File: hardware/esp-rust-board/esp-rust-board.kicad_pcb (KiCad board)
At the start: 2 copper layers, 22.9 x 63.5 mm, 96 parts, among them J1 USB4105-GF-A, Q1 DMG3415U, SW1 SW_Push, SW2 SW_Push, U1 SHTC3, U2 ICM-42670-P, U3 ESP32-C3-MINI-1, U4 Rust_Board, U5 SY8088, U6 MCP73831T-2ACI/OT, Y1 32.768Hz

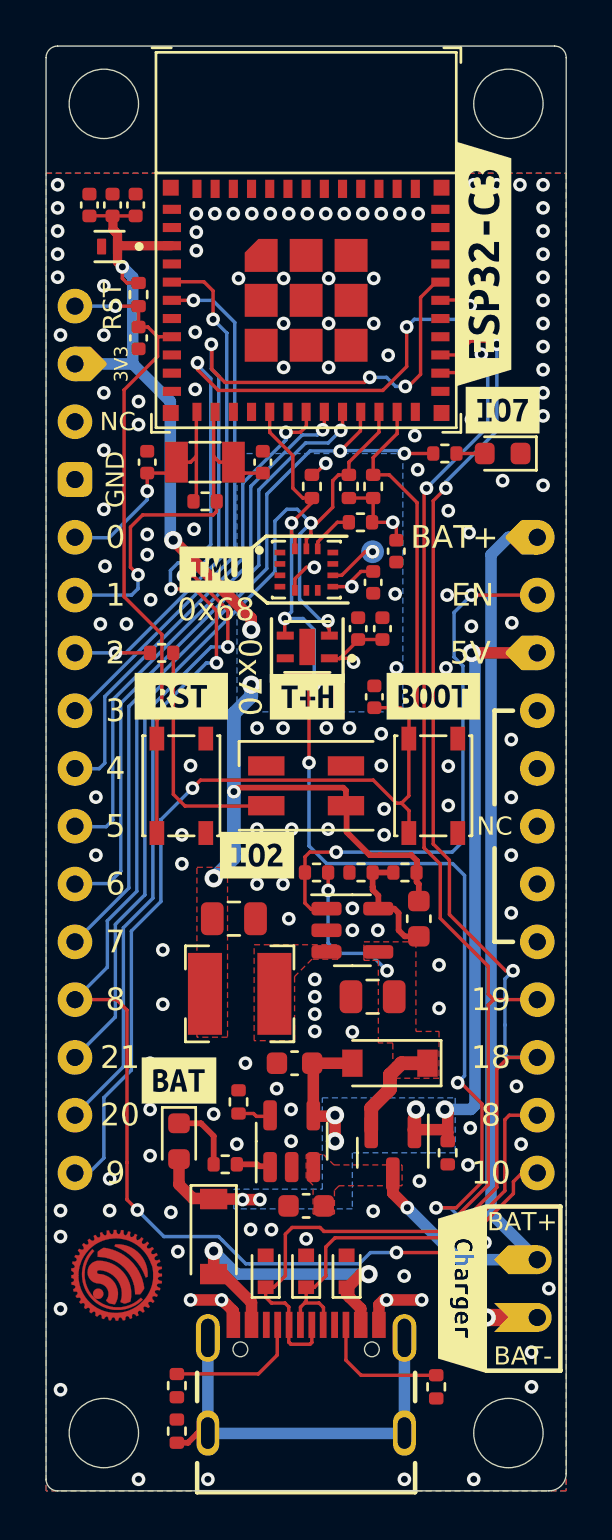
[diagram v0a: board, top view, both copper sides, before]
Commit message: Added LIS3DH
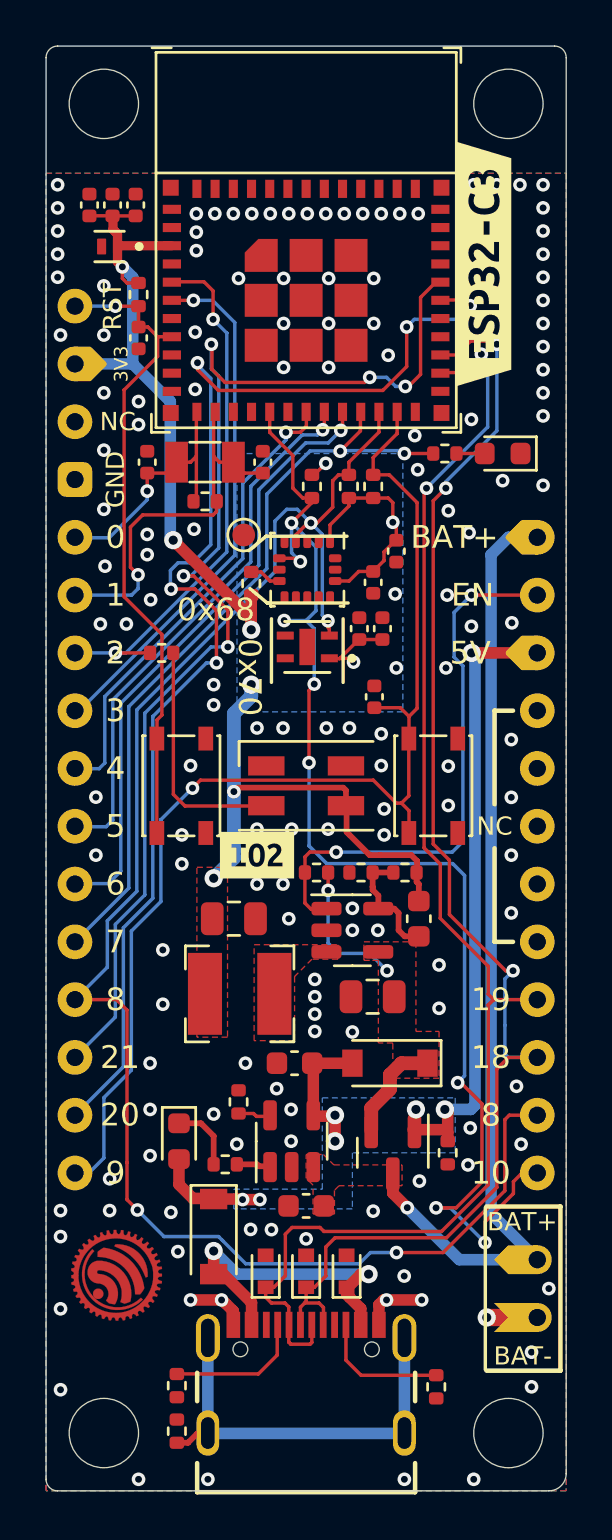
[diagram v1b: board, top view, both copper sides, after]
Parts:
- removed the G*** at (148.1, 70.6)
- removed REF**: logo_HF, Rust_Board:logo_HF
- removed REF**: logo_HF, Rust_Board:logo_PB
- removed kibuzzard-61B9CCBB, kibuzzard-61B9CE3D, kibuzzard-61B9CE86, kibuzzard-61B9CEAB, kibuzzard-61B9EF98, kibuzzard-61C05335, kibuzzard-61C057D5, kibuzzard-61C057FD, kibuzzard-61C05804, kibuzzard-61C0588C, kibuzzard-61C05909, kibuzzard-61C05949, kibuzzard-61C05975, kibuzzard-61C0597E, kibuzzard-61C05A1A, kibuzzard-61C05A22, kibuzzard-61C05B60, kibuzzard-61C05BAC, kibuzzard-61C05C0D, kibuzzard-61C05C87, kibuzzard-61C05C92, kibuzzard-61C05D58, kibuzzard-61C05D75, kibuzzard-61C05DB0, kibuzzard-61C0F315, kibuzzard-61C0F325, kibuzzard-61C0F363, kibuzzard-61C0F3FF, kibuzzard-61C0F406, kibuzzard-61C0F511, kibuzzard-61C0F551: G***, label
- TP2: moved to F.Cu
- U2: value ICM-42670-P -> LIS3DH; footprint Rust_Board:IC_ICM-42670-P -> Package_LGA:LGA-16_3x3mm_P0.5mm_LayoutBorder3x5y
- moved TP2 5.71 mm to (145.3, 86.5), turned to 180 degrees
- moved R7 5.50 mm to (145.7, 88.6), turned to 90 degrees
- moved C3 0.05 mm to (150.4, 90.6)
- turned U2 to -90 degrees
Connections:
- R7 pad 1: Net-(R7-Pad1) -> +3V3
- R7 pad 2: +3V3 -> Net-(R7-Pad2)
- U2 pad 1: GND -> +3V3
- U2 pad 10: unconnected-(U2-Pad10) -> GND
- U2 pad 12: Net-(R7-Pad1) -> GND
- U2 pad 13: IO8_SCL -> unconnected-(U2-Pad13)
- U2 pad 14: IO10_SDA -> +3V3
- U2 pad 4: unconnected-(U2-Pad4) -> IO8_SCL
- U2 pad 5: +3V3 -> GND
- U2 pad 6: GND -> IO10_SDA
- U2 pad 7: GND -> unconnected-(U2-Pad7)
- U2 pad 8: +3V3 -> Net-(R7-Pad2)
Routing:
- net +3V3: track 63.0 -> 66.5 mm, vias 11 -> 9
- net Net-(R7-Pad1): track 2.03 -> 0.00 mm
- net Net-(TP2-Pad1): track 2.18 -> 0.19 mm, vias 1 -> 0
- net IO10_SDA: track 54.8 -> 56.3 mm, vias 7 -> 8
- net Net-(R7-Pad2): track 0.00 -> 1.43 mm
- net IO8_SCL: track 74.8 -> 74.2 mm

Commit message: Sync
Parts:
- removed TP2: IMU_INT2, TestPoint:TestPoint_Pad_D1.0mm
- added G***: LOGO, Rust_Board:esp-rs_logo_tiny, B.Cu at (148.1, 70.6)
- added REF**: logo_HF, Rust_Board:logo_HF, B.Cu at (149.7, 126.0)
- added REF**: logo_HF, Rust_Board:logo_PB, B.Cu at (146.4, 126.0)
- added kibuzzard-61B9CE3D: G***, label, B.Cu at (148.1, 93.5)
- added kibuzzard-61B9CE86: G***, label, F.Cu at (153.7, 93.6)
- added kibuzzard-61B9CEAB: G***, label, F.Cu at (142.6, 93.6)
- added kibuzzard-61B9EF98: G***, label, F.Cu at (156.7, 81.0)
- added kibuzzard-61C05335: G***, label, F.Cu at (142.5, 110.5)
- added kibuzzard-61C057D5: G***, label, B.Cu at (142.0, 86.6)
- added kibuzzard-61C057FD: G***, label, B.Cu at (142.0, 89.2)
- added kibuzzard-61C05804: G***, label, B.Cu at (142.0, 91.7)
- added kibuzzard-61C0588C: G***, label, B.Cu at (142.0, 94.2)
- added kibuzzard-61C05909: G***, label, B.Cu at (153.2, 114.6)
- added kibuzzard-61C05949: G***, label, B.Cu at (153.2, 112.0)
- added kibuzzard-61C05975: G***, label, B.Cu at (153.2, 109.5)
- added kibuzzard-61C0597E: G***, label, B.Cu at (153.2, 106.9)
- added kibuzzard-61C05A22: G***, label, F.Cu at (148.1, 93.6)
- added kibuzzard-61C05B60: G***, label, B.Cu at (154.2, 86.6)
- added kibuzzard-61C05BAC: G***, label, B.Cu at (154.2, 91.7)
- added kibuzzard-61C05C0D: G***, label, B.Cu at (154.2, 89.2)
- added kibuzzard-61C05C87: G***, label, B.Cu at (142.0, 79.0)
- added kibuzzard-61C05C92: G***, label, B.Cu at (141.9, 76.5)
- added kibuzzard-61C05D58: G***, label, B.Cu at (142.5, 109.5)
- added kibuzzard-61C05D75: G***, label, B.Cu at (142.5, 112.0)
- added kibuzzard-61C05DB0: G***, label, B.Cu at (143.0, 114.6)
- added kibuzzard-61C0F315: G***, label, B.Cu at (142.0, 96.8)
- added kibuzzard-61C0F325: G***, label, B.Cu at (142.0, 99.3)
- added kibuzzard-61C0F363: G***, label, B.Cu at (156.0, 99.3)
- added kibuzzard-61C0F3FF: G***, label, B.Cu at (154.7, 120.9)
- added kibuzzard-61C0F406: G***, label, B.Cu at (154.7, 118.4)
- added kibuzzard-61C0F511, kibuzzard-61C0F551: G***, label, F.Cu at (154.9, 119.6)
- added kibuzzard-62974DD1: G***, kibuzzard-62974DD1, F.Cu at (144.6, 87.6)
- added kibuzzard-6297573C: G***, kibuzzard-6297573C, B.Cu at (148.1, 85.4)
- added kibuzzard-62975A90: G***, kibuzzard-62975A90, F.Cu at (141.5, 104.1)
- moved R7 5.85 mm to (151.0, 86.3), turned to -90 degrees
- moved J1 1.22 mm to (148.1, 124.8)
- moved C2 0.63 mm to (150.4, 88.7)
- moved R19 0.16 mm to (151.0, 84.2)
- moved R17 0.15 mm to (150.0, 84.2)
- moved U2 0.10 mm to (148.1, 88.1), turned to 90 degrees
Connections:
- U2 pad 7: unconnected-(U2-Pad7) -> +3V3
- U2 pad 9: Net-(TP2-Pad1) -> unconnected-(U2-Pad9)
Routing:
- net +3V3: track 66.5 -> 62.2 mm, vias 9 -> 11
- net Net-(R7-Pad2): track 1.43 -> 2.01 mm
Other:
- board text added: "0x19"
- board text added: "2022-06-01"
- board text added: "2222"
- board text added: "ESP32-C3-DevKit-RUST-1 - EW22 Version"
- board text added: "ESP32-C3-DevKit-RUST-1 v1.2b 06/2022"
- board text added: "Rev 1.2b"
- board text removed: "0x68"
- board text removed: "2022-04-27"
- board text removed: "2217"
- board text removed: "ESP32-C3-DevKit-RUST-1"
- board text removed: "ESP32-C3-DevKit-RUST-1 v1.2a 04/2022"
- board text removed: "Rev 1.2a"
